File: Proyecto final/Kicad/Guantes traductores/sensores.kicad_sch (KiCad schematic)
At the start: 4 parts, among them U2 ADS7128IRTER

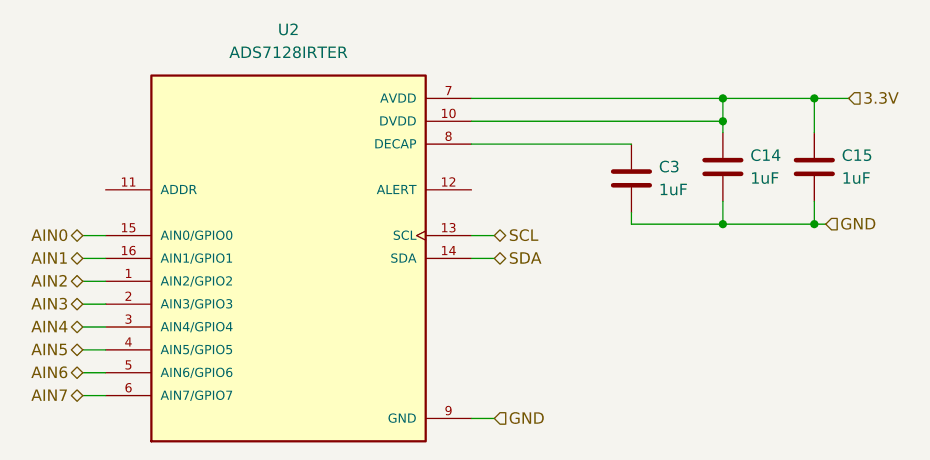
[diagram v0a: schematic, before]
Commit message: Posicion de componentes
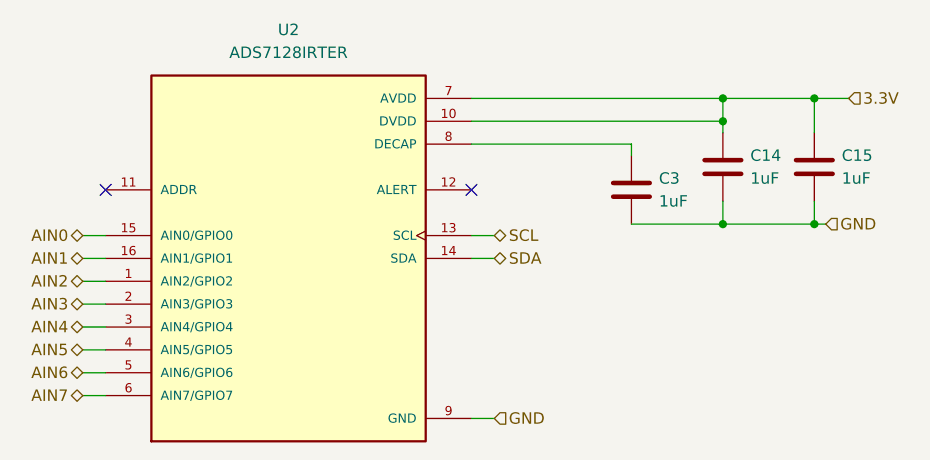
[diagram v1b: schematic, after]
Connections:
- no-connect marks 0 -> 2
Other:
- moved on the sheet: C3
